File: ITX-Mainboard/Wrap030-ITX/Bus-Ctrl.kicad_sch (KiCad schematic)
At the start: 20 parts, among them U3 74HCT04

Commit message: Schematic substantial completion
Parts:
- added C1: 100nF, Capacitor_SMD:C_0402_1005Metric_Pad0.74x0.62mm_HandSolder, symbol Device:C_Small
- added D8: LED, LED_THT:LED_D3.0mm, symbol Device:LED
- added J9: Conn_01x02, Connector_PinHeader_2.54mm:PinHeader_1x02_P2.54mm_Vertical, symbol Connector_Generic:Conn_01x02
- added SW1: SW_Push, Button_Switch_THT:SW_PUSH_6mm, symbol Switch:SW_Push
- added U23: 74LS148, Package_DIP:DIP-16_W7.62mm_Socket, symbol 74xx:74LS148
- added U9: DS1813-5+T&R, Package_TO_SOT_THT:TO-92_Inline, symbol Wrap030-ITX:DS1813
- C1: footprint Capacitor_SMD:C_0805_2012Metric -> Capacitor_SMD:C_0402_1005Metric_Pad0.74x0.62mm_HandSolder; JLC-Part (none) -> https://jlcpcb.com/partdetail/1877-CL05B104KO5NNNC/C1525
- C15: footprint Capacitor_SMD:C_0805_2012Metric -> Capacitor_SMD:C_0402_1005Metric_Pad0.74x0.62mm_HandSolder; JLC-Part (none) -> https://jlcpcb.com/partdetail/53938-CL05A105KA5NQNC/C52923
- RN1: Mouser-Part (none) -> 603-YC124-JR-07220RL; Notes (none) -> 220R x4
- U3: footprint (none) -> Package_DIP:DIP-14_W7.62mm_Socket
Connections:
- net GND: now also C1.2, D8.1 (K), J9.1 (Pin_1), SW1.2, U23.5 (EI), U23.8 (GND), U9.3 (GND)
- net VCC: now also C1.1, U23.16 (VCC), U9.2 (VCC)
- net ~{IPL0}: now also U23.9 (S0)
- net ~{IPL1}: now also U23.7 (S1)
- net ~{IPL2}: now also U23.6 (S2)
- net ~{RESET}: now also J9.2 (Pin_2), SW1.1, U9.1 (~{RESET})
- net ~{ISA-CE}: now reaches VGEN1.24 (IO46)
- net ~{ISA-CE}: now also U3.13
- net ~{ISA-DACK16}: now reaches VGEN1.40 (IO51)
- net ~{ISA-DACK8}: now reaches VGEN1.41 (IO49)
- net PWR_OK: now reaches VGEN1.54 (IO83)
- net PWR_ON_L: now reaches VGEN1.55 (IO85)
- net ~{SPIO-CE}: now reaches VGEN1.56 (IO86)
- net ~{PS2-ATN}: now reaches VGEN1.57 (IO88)
- net ~{PS2-ACK}: now reaches VGEN1.58 (IO91)
- net +5VP: now reaches RN1.4 (R4.1)
- net at RN1.5 (R4.2): now also D8.2 (A)

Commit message: PCB substantial completion
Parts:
- removed U23: 74LS148, Package_DIP:DIP-16_W7.62mm_Socket, symbol 74xx:74LS148
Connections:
- net CPU-A0: now also VGEN1.81 (IO128); no longer VGEN1.65 (IO101)
- net CPU-A1: now also VGEN1.80 (IO126); no longer VGEN1.67 (IO104)
- net CPU-A21: now also VGEN1.54 (IO83); no longer VGEN1.68 (IO105)
- net CPU-A22: now also VGEN1.55 (IO85); no longer VGEN1.69 (IO107)
- net CPU-A23: now also VGEN1.52 (IO80); no longer VGEN1.70 (IO109)
- net CPU-A24: now also VGEN1.24 (IO46); no longer VGEN1.73 (IO115)
- net CPU-A25: now also VGEN1.27 (IO43); no longer VGEN1.74 (IO117)
- net CPU-A26: now also VGEN1.22 (IO17); no longer VGEN1.75 (IO118)
- net CPU-A27: now also VGEN1.25 (IO45); no longer VGEN1.76 (IO120)
- net CPU-A28: now also VGEN1.18 (IO24); no longer VGEN1.77 (IO123)
- net CPU-A29: now also VGEN1.20 (IO21); no longer VGEN1.79 (IO125)
- net CPU-A30: now also VGEN1.16 (IO27); no longer VGEN1.80 (IO126)
- net CPU-A31: now also VGEN1.17 (IO25); no longer VGEN1.81 (IO128)
- net CPU-D24: now also VGEN1.28 (IO40); no longer VGEN1.44 (IO65)
- net CPU-D25: now also VGEN1.30 (IO37); no longer VGEN1.45 (IO67)
- net CPU-D26: now also VGEN1.29 (IO38); no longer VGEN1.46 (IO69)
- net CPU-D27: now also VGEN1.31 (IO35); no longer VGEN1.48 (IO72)
- net CPU-D28: now also VGEN1.34 (IO61); no longer VGEN1.49 (IO73)
- net CPU-D29: now also VGEN1.33 (IO64); no longer VGEN1.50 (IO75)
- net CPU-D30: now also VGEN1.35 (IO59); no longer VGEN1.51 (IO77)
- net CPU-D31: now also VGEN1.36 (IO57); no longer VGEN1.52 (IO80)
- net FC1: now also VGEN1.15 (IO29); no longer VGEN1.11 (IO5)
- net FC2: now also VGEN1.11 (IO5); no longer VGEN1.10 (IO6)
- net PWR_OK: now also VGEN1.5 (IO14); no longer VGEN1.54 (IO83)
- net PWR_ON_L: now also VGEN1.4 (IO16); no longer VGEN1.55 (IO85)
- net R/~{W}: now also VGEN1.58 (IO91); no longer VGEN1.4 (IO16)
- net SIZ0: now also VGEN1.76 (IO120); no longer VGEN1.9 (IO8)
- net SIZ1: now also VGEN1.75 (IO118); no longer VGEN1.8 (IO11)
- net ~{AS}: now also VGEN1.40 (IO51); no longer VGEN1.6 (IO13)
- net ~{AVEC}: now also VGEN1.10 (IO6); no longer VGEN1.25 (IO45)
- net ~{BERR}: now also U3.3, VGEN1.73 (IO115); no longer U3.5, VGEN1.18 (IO24)
- net ~{CIIN}: now also VGEN1.56 (IO86); no longer VGEN1.17 (IO25)
- net ~{DSACK0}: now also VGEN1.9 (IO8); no longer VGEN1.22 (IO17)
- net ~{DSACK1}: now also VGEN1.8 (IO11); no longer VGEN1.21 (IO19)
- net ~{DS}: now also VGEN1.41 (IO49); no longer VGEN1.5 (IO14)
- net ~{FPU-CE}: now also VGEN1.49 (IO73); no longer VGEN1.34 (IO61)
- net ~{FPU-SENSE}: now also VGEN1.50 (IO75); no longer VGEN1.33 (IO64)
- net ~{HALT}: now also U3.1; no longer U3.3
- net ~{IPL0}: now also VGEN1.65 (IO101); no longer VGEN1.29 (IO38)
- net ~{IPL1}: now also VGEN1.67 (IO104); no longer VGEN1.28 (IO40)
- net ~{IPL2}: now also VGEN1.68 (IO105); no longer VGEN1.27 (IO43)
- net ~{ISA-CE}: now also VGEN1.74 (IO117); no longer VGEN1.24 (IO46)
- net ~{ISA-DACK16}: now also VGEN1.69 (IO107); no longer VGEN1.40 (IO51)
- net ~{ISA-DACK8}: now also VGEN1.70 (IO109); no longer VGEN1.41 (IO49)
- net ~{MEM-RD}: now also VGEN1.48 (IO72); no longer VGEN1.16 (IO27)
- net ~{MEM-WR}: now also VGEN1.46 (IO69); no longer VGEN1.15 (IO29)
- net ~{PS2-ACK}: now also VGEN1.57 (IO88); no longer VGEN1.58 (IO91)
- net ~{PS2-ATN}: now also VGEN1.60 (IO93); no longer VGEN1.57 (IO88)
- net ~{RAM-CE}: now also VGEN1.79 (IO125); no longer VGEN1.35 (IO59)
- net ~{RAM-DSACK}: now also VGEN1.77 (IO123); no longer VGEN1.36 (IO57)
- net ~{RESET}: now also U3.5; no longer U3.1
- net ~{ROM-CE}: now also VGEN1.44 (IO65); no longer VGEN1.31 (IO35)
- net ~{SPIO-CE}: now also VGEN1.64 (IO99); no longer VGEN1.56 (IO86)
- net ~{STERM}: now also VGEN1.6 (IO13); no longer VGEN1.20 (IO21)
- net ~{VID-CE}: now also VGEN1.45 (IO67); no longer VGEN1.30 (IO37), VGEN1.39 (IO53)
- net ~{VID-DSACK}: now also VGEN1.63 (IO97); no longer VGEN1.37 (IO56)
- net BERR-LED: now reaches D3.2 (A), RN1.6 (R3.2)
- net RAM-LED: now reaches D6.2 (A), RN1.7 (R2.2)
- net HALT-LED: now reaches D4.2 (A), RN1.5 (R4.2)
- net PWR-LED: now reaches D1.2 (A), RN1.8 (R1.2)
- net RAM-LED-R: now reaches RN1.2 (R2.1), U3.10
- net BERR-LED-R: now reaches RN1.3 (R3.1), U3.4
- net ROM-LED: now reaches D5.2 (A), RN1.8 (R1.2)
- net HALT-LED-R: now reaches RN1.4 (R4.1)
- net HALT-LED-R: now also U3.2; no longer U3.6
- net ROM-LED-R: now reaches RN1.1 (R1.1), U3.8
- net ISA-LED-R: now reaches RN1.3 (R3.1), U3.12
- net DEBUG-LED: now reaches D8.2 (A), RN1.5 (R4.2)
- net ISA-LED: now reaches D7.2 (A), RN1.6 (R3.2)
- net RESET-LED: now reaches D2.2 (A), RN1.7 (R2.2)
- net RESET-LED-R: now reaches RN1.2 (R2.1)
- net RESET-LED-R: now also U3.6; no longer U3.2
- net +5VP renamed DEBUG-LED-R
- net DEBUG-LED-R: now also VGEN1.21 (IO19)
- new net ~{BUS-DSACK0}: VGEN1.37 (IO56)
- new net ~{BUS-DSACK1}: VGEN1.39 (IO53)
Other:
- moved on the sheet: U3A, U3C

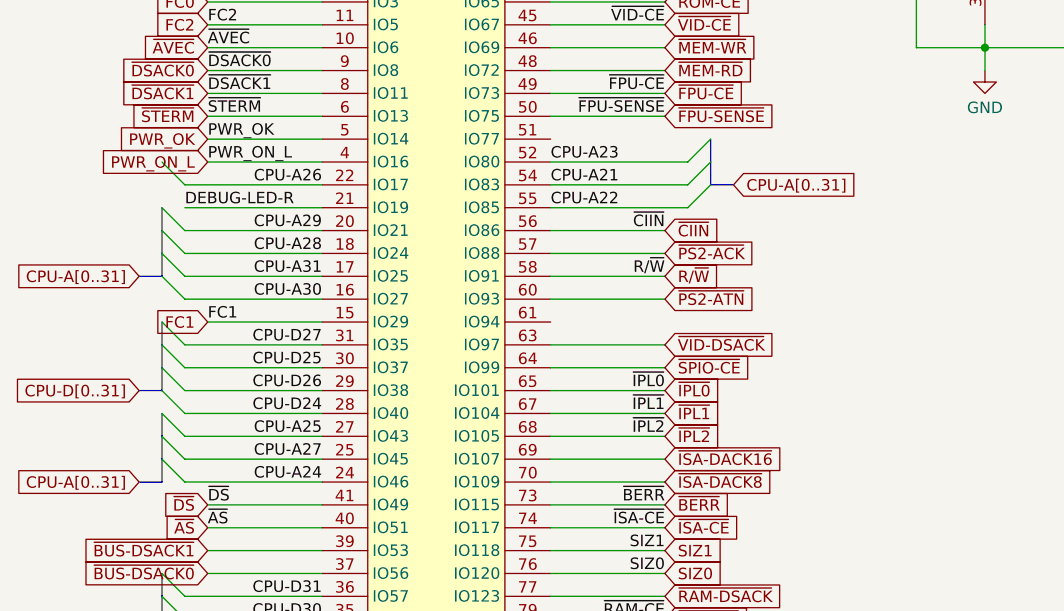
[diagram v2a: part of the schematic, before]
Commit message: Add interrupt controller to schematic
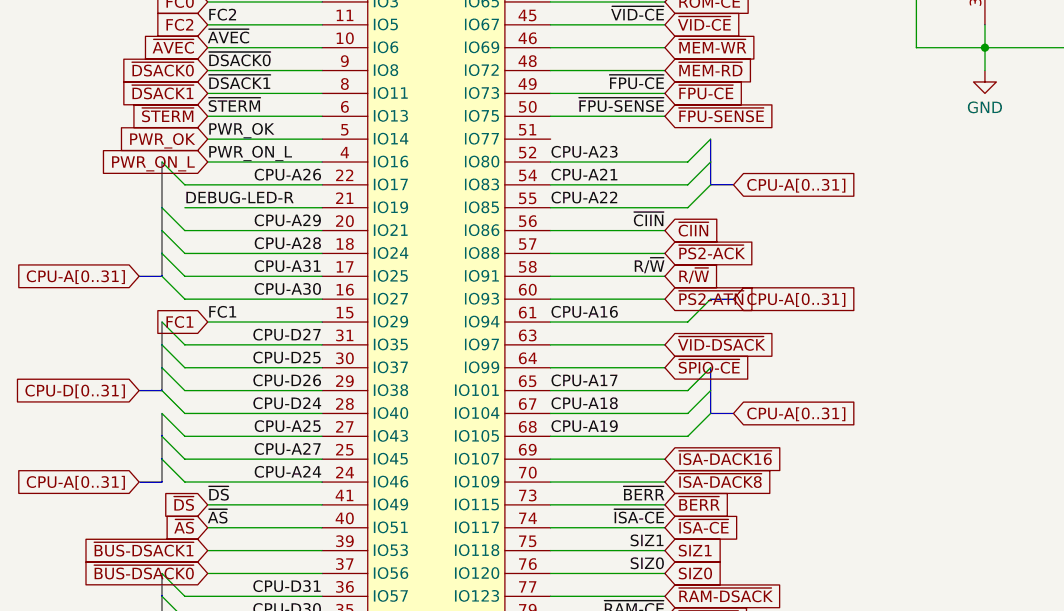
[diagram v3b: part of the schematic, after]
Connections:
- net CPU-A16: now reaches VGEN1.61 (IO94)
- net ~{IPL0} renamed CPU-A17
- net ~{IPL1} renamed CPU-A18
- net ~{IPL2} renamed CPU-A19
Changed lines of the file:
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@@
+    (stroke (width 0) (type default))
+  )
+  (bus_entry (at 93.98 93.98) (size -2.54 2.54)
     (stroke (width 0) (type default))
   )
@@
     (stroke (width 0) (type default))
   )
+  (bus_entry (at 93.98 83.82) (size -2.54 2.54)
+    (stroke (width 0) (type default))
+  )
   (bus_entry (at 33.02 86.36) (size 2.54 2.54)
     (stroke (width 0) (type default))
@@
     (stroke (width 0) (type default))
   )
+  (bus_entry (at 93.98 91.44) (size -2.54 2.54)
+    (stroke (width 0) (type default))
+  )
   (bus_entry (at 93.98 71.12) (size -2.54 2.54)
     (stroke (width 0) (type default))
@@
     (stroke (width 0) (type default))
   )
+  (bus_entry (at 93.98 96.52) (size -2.54 2.54)
+    (stroke (width 0) (type default))
+  )
   (bus_entry (at 33.02 73.66) (size 2.54 2.54)
     (stroke (width 0) (type default))
@@
     (stroke (width 0) (type default))
   )
+  (wire (pts (xy 76.2 93.98) (xy 91.44 93.98))
+    (stroke (width 0) (type default))
+  )
   (bus (pts (xy 33.02 114.3) (xy 33.02 116.84))
     (stroke (width 0) (type default))
@@
     (stroke (width 0) (type default))
   )
-  (wire (pts (xy 88.9 99.06) (xy 76.2 99.06))
-    (stroke (width 0) (type default))
-  )
   (wire (pts (xy 210.82 27.94) (xy 218.44 27.94))
     (stroke (width 0) (type default))
   )
+  (wire (pts (xy 76.2 99.06) (xy 91.44 99.06))
+    (stroke (width 0) (type default))
+  )
   (wire (pts (xy 78.74 162.56) (xy 78.74 165.1))
     (stroke (width 0) (type default))
@@
     (stroke (width 0) (type default))
   )
-  (wire (pts (xy 88.9 93.98) (xy 76.2 93.98))
-    (stroke (width 0) (type default))
-  )
   (wire (pts (xy 208.28 25.4) (xy 218.44 25.4))
     (stroke (width 0) (type default))
@@
     (stroke (width 0) (type default))
   )
+  (bus (pts (xy 33.02 68.58) (xy 33.02 73.66))
+    (stroke (width 0) (type default))
+  )
   (wire (pts (xy 210.82 66.04) (xy 218.44 66.04))
     (stroke (width 0) (type default))
@@
     (stroke (width 0) (type default))
   )
+  (wire (pts (xy 76.2 96.52) (xy 91.44 96.52))
+    (stroke (width 0) (type default))
+  )
   (wire (pts (xy 213.36 68.58) (xy 218.44 68.58))
     (stroke (width 0) (type default))
@@
     (stroke (width 0) (type default))
   )
+  (wire (pts (xy 76.2 86.36) (xy 91.44 86.36))
+    (stroke (width 0) (type default))
+  )
   (wire (pts (xy 116.84 55.88) (xy 124.46 55.88))
     (stroke (width 0) (type default))
@@
     (stroke (width 0) (type default))
   )
+  (bus (pts (xy 93.98 91.44) (xy 93.98 93.98))
+    (stroke (width 0) (type default))
+  )
   (wire (pts (xy 76.2 162.56) (xy 78.74 162.56))
     (stroke (width 0) (type default))
@@
     (stroke (width 0) (type default))
   )
+  (bus (pts (xy 93.98 83.82) (xy 96.52 83.82))
+    (stroke (width 0) (type default))
+  )
   (wire (pts (xy 76.2 147.32) (xy 78.74 147.32))
     (stroke (width 0) (type default))
@@
     (stroke (width 0) (type default))
   )
+  (bus (pts (xy 93.98 96.52) (xy 96.52 96.52))
+    (stroke (width 0) (type default))
+  )
   (wire (pts (xy 210.82 76.2) (xy 210.82 66.04))
     (stroke (width 0) (type default))
@@
     (stroke (width 0) (type default))
   )
-  (wire (pts (xy 88.9 96.52) (xy 76.2 96.52))
+  (bus (pts (xy 93.98 93.98) (xy 93.98 96.52))
     (stroke (width 0) (type default))
   )
@@
     (effects (font (size 1.27 1.27)) (justify left bottom))
   )
-  (label "~{IPL0}" (at 88.9 93.98 180) (fields_autoplaced)
-    (effects (font (size 1.27 1.27)) (justify right bottom))
-  )
   (label "SIZ1" (at 88.9 111.76 180) (fields_autoplaced)
     (effects (font (size 1.27 1.27)) (justify right bottom))
@@
     (effects (font (size 1.27 1.27)) (justify right bottom))
   )
+  (label "CPU-A17" (at 76.2 93.98 0)
+    (effects (font (size 1.27 1.27)) (justify left bottom))
+  )
   (label "CPU-A25" (at 50.8 99.06 180) (fields_autoplaced)
     (effects (font (size 1.27 1.27)) (justify right bottom))
@@
     (effects (font (size 1.27 1.27)) (justify left bottom))
   )
+  (label "CPU-A16" (at 76.2 86.36 0)
+    (effects (font (size 1.27 1.27)) (justify left bottom))
+  )
   (label "BERR-LED-R" (at 218.44 27.94 180) (fields_autoplaced)
     (effects (font (size 1.27 1.27)) (justify right bottom))
@@
     (effects (font (size 1.27 1.27)) (justify right bottom))
   )
+  (label "CPU-A19" (at 76.2 99.06 0)
+    (effects (font (size 1.27 1.27)) (justify left bottom))
+  )
   (label "SIZ0" (at 88.9 114.3 180) (fields_autoplaced)
     (effects (font (size 1.27 1.27)) (justify right bottom))
@@
     (effects (font (size 1.27 1.27)) (justify left bottom))
   )
+  (label "CPU-A18" (at 76.2 96.52 0)
+    (effects (font (size 1.27 1.27)) (justify left bottom))
+  )
   (label "CPU-A26" (at 50.8 71.12 180) (fields_autoplaced)
     (effects (font (size 1.27 1.27)) (justify right bottom))
@@
     (effects (font (size 1.27 1.27)) (justify right bottom))
   )
-  (label "~{IPL1}" (at 88.9 96.52 180) (fields_autoplaced)
-    (effects (font (size 1.27 1.27)) (justify right bottom))
-  )
   (label "CPU-D27" (at 50.8 88.9 180) (fields_autoplaced)
-    (effects (font (size 1.27 1.27)) (justify right bottom))
-  )
-  (label "~{IPL2}" (at 88.9 99.06 180) (fields_autoplaced)
     (effects (font (size 1.27 1.27)) (justify right bottom))
   )
@@
     )
   )
+  (global_label "CPU-A[0..31]" (shape input) (at 96.52 96.52 0) (fields_autoplaced)
+    (effects (font (size 1.27 1.27)) (justify left))
+    (property "Intersheetrefs" "${INTERSHEET_REFS}" (at 112.4888 96.52 0)
+      (effects (font (size 1.27 1.27)) (justify left) hide)
+    )
+  )
   (global_label "~{FPU-SENSE}" (shape input) (at 88.9 63.5 0) (fields_autoplaced)
     (effects (font (size 1.27 1.27)) (justify left))
@@
     )
   )
-  (global_label "~{IPL1}" (shape input) (at 88.9 96.52 0) (fields_autoplaced)
-    (effects (font (size 1.27 1.27)) (justify left))
-    (property "Intersheetrefs" "${INTERSHEET_REFS}" (at 95.9182 96.52 0)
-      (effects (font (size 1.27 1.27)) (justify left) hide)
-    )
-  )
   (global_label "~{CIIN}" (shape input) (at 88.9 76.2 0) (fields_autoplaced)
     (effects (font (size 1.27 1.27)) (justify left))
@@
     )
   )
-  (global_label "~{IPL0}" (shape input) (at 88.9 93.98 0) (fields_autoplaced)
-    (effects (font (size 1.27 1.27)) (justify left))
-    (property "Intersheetrefs" "${INTERSHEET_REFS}" (at 95.9182 93.98 0)
-      (effects (font (size 1.27 1.27)) (justify left) hide)
-    )
-  )
   (global_label "~{ISA-DACK16}" (shape input) (at 88.9 101.6 0) (fields_autoplaced)
     (effects (font (size 1.27 1.27)) (justify left))
@@
     )
   )
-  (global_label "~{IPL2}" (shape input) (at 88.9 99.06 0) (fields_autoplaced)
-    (effects (font (size 1.27 1.27)) (justify left))
-    (property "Intersheetrefs" "${INTERSHEET_REFS}" (at 95.9182 99.06 0)
-      (effects (font (size 1.27 1.27)) (justify left) hide)
-    )
-  )
   (global_label "~{VID-CE}" (shape input) (at 88.9 53.34 0) (fields_autoplaced)
     (effects (font (size 1.27 1.27)) (justify left))
@@
       (effects (font (size 1.27 1.27)) (justify left) hide)
     )
+  )
+  (global_label "CPU-A[0..31]" (shape input) (at 96.52 83.82 0) (fields_autoplaced)
+    (effects (font (size 1.27 1.27)) (justify left))
+    (property "Intersheetrefs" "${INTERSHEET_REFS}" (at 112.4888 83.82 0)
+      (effects (font (size 1.27 1.27)) (justify left) hide)
+    )

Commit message: Completing PCB Routing
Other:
- title: Wrap030 ITX -> Wrap030-ATX Mainboard
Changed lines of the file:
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@@
   (paper "USLetter")
   (title_block
-    (title "Wrap030 ITX")
-    (date "2023-03-15")
-    (rev "0")
+    (title "Wrap030-ATX Mainboard")
+    (date "2023-03-26")
+    (rev "1")
     (company "techav")
   )
@@
     (effects (font (size 1.27 1.27)) (justify right bottom))
   )
-  (label "CPU-A17" (at 76.2 93.98 0)
+  (label "CPU-A17" (at 76.2 93.98 0) (fields_autoplaced)
     (effects (font (size 1.27 1.27)) (justify left bottom))
   )
@@
     (effects (font (size 1.27 1.27)) (justify left bottom))
   )
-  (label "CPU-A16" (at 76.2 86.36 0)
+  (label "CPU-A16" (at 76.2 86.36 0) (fields_autoplaced)
     (effects (font (size 1.27 1.27)) (justify left bottom))
   )
@@
     (effects (font (size 1.27 1.27)) (justify right bottom))
   )
-  (label "CPU-A19" (at 76.2 99.06 0)
+  (label "CPU-A19" (at 76.2 99.06 0) (fields_autoplaced)
     (effects (font (size 1.27 1.27)) (justify left bottom))
   )
@@
     (effects (font (size 1.27 1.27)) (justify left bottom))
   )
-  (label "CPU-A18" (at 76.2 96.52 0)
-    (effects (font (size 1.27 1.27)) (justify left bottom))
-  )
+  (label "CPU-A18" (at 76.2 96.52 0) (fields_autoplaced)
+    (effects (font (size 1.27 1.27)) (justify left bottom))
+  )
